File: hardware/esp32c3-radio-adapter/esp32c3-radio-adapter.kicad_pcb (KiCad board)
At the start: 2 copper layers, 27 x 36.5 mm, 7 parts, among them J1 Conn_01x08, J2 Conn_01x08, J3 SX1278_Ra-02

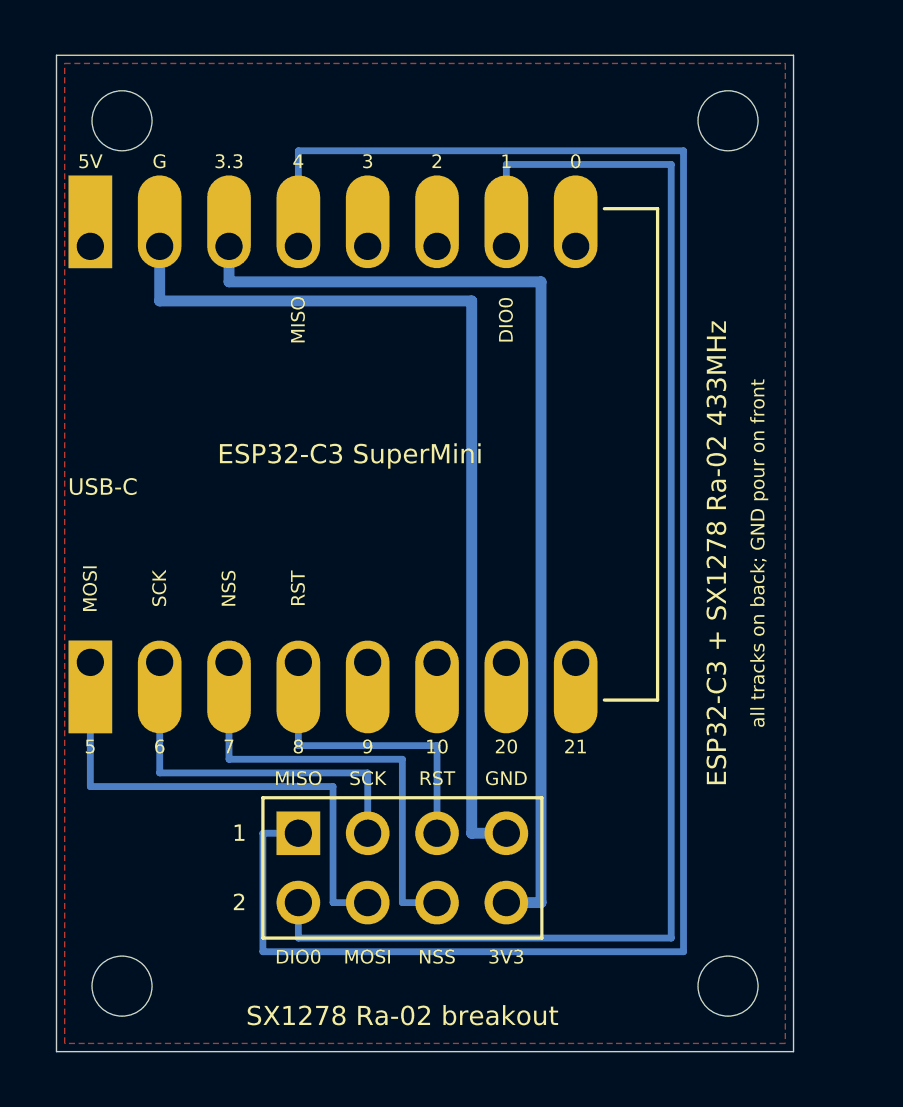
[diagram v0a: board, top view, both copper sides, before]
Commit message: Merge the two socket adapters into esp32c3-radio-adapter; two-sided pin silk on the replicas
* esp32c3-radio-adapter replaces esp32c3-cc1101-adapter and
  esp32c3-ra02-adapter: the E07-M1101D and Ra-02 breakout headers differ
  only at outer column 3 (GDO0 / RST) and inner column 1 (GDO2 / DIO0),
  wired to GPIO10 and GPIO3, so one socket takes either board.  Nets are
  named GDO0_RST, GDO2_DIO0 and CSN_NSS; the silk carries the E07 names
  with the Ra-02 names in parentheses, plus both boards' fab outlines.
* Ra-02 breakout replica: header and module pin numbers on the back silk;
  header pin names beside each column on both sides.
* E07-M1101D replica: pin names beside each column on both sides; the
  markers, box and legend are mirrored onto the back.
* Pinout diagrams combined into docs/images/pinout-radio-boards.svg.
* README, export defaults and generator lists updated.

Co-Authored-By: Claude Fable 5.1 <noreply@anthropic.com>
Claude-Session: https://claude.ai/code/session_01JoGdh4Cg3VtTTDZi4gQuiN
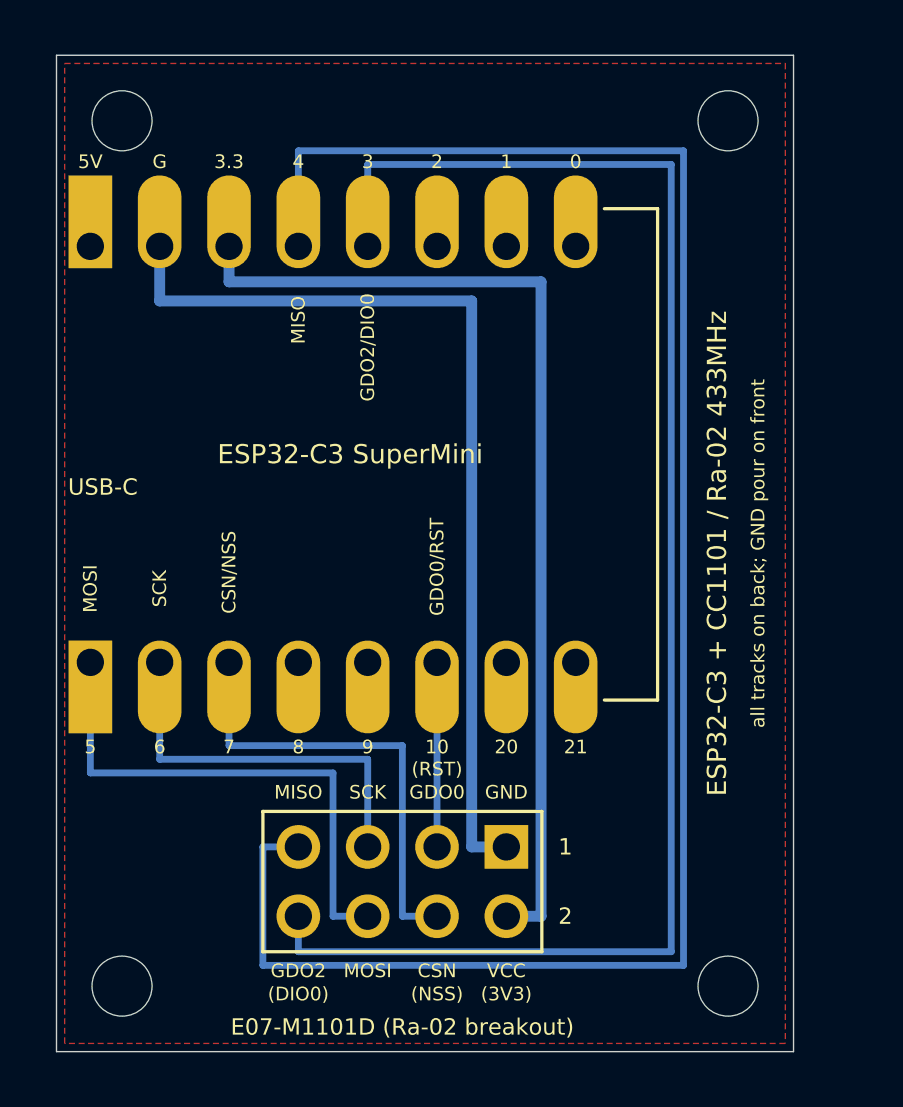
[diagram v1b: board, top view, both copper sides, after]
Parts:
- J3: value SX1278_Ra-02 -> E07-M1101D_or_Ra-02; footprint Adapter:PinSocket_2x04_P2.54mm_Ra02_Breakout -> Adapter:PinSocket_2x04_P2.54mm_E07
- moved J3 7.64 mm to (116.5, 129.0)
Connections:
- J1 pad 3: NSS -> CSN_NSS
- J1 pad 4: RESET -> GPIO8
- J1 pad 6: GPIO10 -> GDO0_RST
- J2 pad 5: GPIO3 -> GDO2_DIO0
- J2 pad 7: DIO0 -> GPIO1
- J3 pad 1: MISO -> GND
- J3 pad 2: DIO0 -> +3V3
- J3 pad 3: SCK -> GDO0_RST
- J3 pad 4: MOSI -> CSN_NSS
- J3 pad 5: RESET -> SCK
- J3 pad 6: NSS -> MOSI
- J3 pad 7: GND -> MISO
- J3 pad 8: +3V3 -> GDO2_DIO0
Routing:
- net GDO2_DIO0: track 0.00 -> 57.9 mm
- net DIO0: track 52.3 -> 0.00 mm
- net CSN_NSS: track 0.00 -> 16.9 mm
- net NSS: track 16.4 -> 0.00 mm
- net RESET: track 11.3 -> 0.00 mm
- net GDO0_RST: track 0.00 -> 6.76 mm
- net SCK: track 13.9 -> 14.4 mm
- net MOSI: track 19.0 -> 19.5 mm
- net MISO: track 68.0 -> 68.5 mm
- net GND: track 34.2 -> 34.7 mm
- net +3V3: track 36.7 -> 37.2 mm
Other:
- board text added: "(3V3)"
- board text added: "(DIO0)"
- board text added: "(NSS)"
- board text added: "(RST)"
- board text added: "CSN"
- board text added: "CSN/NSS"
- board text added: "E07-M1101D (Ra-02 breakout)"
- board text added: "ESP32-C3 + CC1101 / Ra-02 433MHz"
- board text added: "GDO0"
- board text added: "GDO0/RST"
- board text added: "GDO2"
- board text added: "GDO2/DIO0"
- board text added: "VCC"
- board text removed: "3V3"
- board text removed: "DIO0"
- board text removed: "ESP32-C3 + SX1278 Ra-02 433MHz"
- board text removed: "NSS"
- board text removed: "RST"
- board text removed: "SX1278 Ra-02 breakout"

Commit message: Adapters: expansion header for the unused SuperMini pins and a radio-type strap
Pin-header adapter:
* J4, a 1x7 2.54 mm header on the top edge, carries every SuperMini pin the
  radio does not use: 5V, GPIO8, GPIO9, GPIO2, GPIO20, GPIO21, GPIO0.  Its
  pins sit at the gaps between the SuperMini's pins so each net reaches it on
  the front copper without crossing another (power-row nets jog above their
  row, GPIO-row nets rise between the rows and pass between the power-row
  pads).  The radio tracks on the back are unchanged; the GND pour flows
  around the new tracks.
* JP1, a two-pad solder jumper right of the SuperMini, straps GPIO1 (net
  RADIO_ID) to GND: open = CC1101 E07-M1101D, bridged = Ra-02 breakout.

SX1278 module adapter: GPIO1 is tied to 3V3 (silk "ID=3V3"), so the same
pin reads high there.  Firmware samples GPIO1 with the internal pull-down
and then the pull-up to tell the three states apart; GPIO1 is not a boot
strapping pin.

The header is 2.3 mm from the top edge so the MISO lane on the back keeps
its clearance under it.  Both adapters pass ERC and DRC; README and the
manufacturing notes describe the header and the strap.

Co-Authored-By: Claude Fable 5.1 <noreply@anthropic.com>
Claude-Session: https://claude.ai/code/session_01JoGdh4Cg3VtTTDZi4gQuiN
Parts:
- added J4: Expansion, Adapter:PinHeader_1x07_P2.54mm_Vertical, F.Cu at (105.0, 102.3)
- added JP1: RA-02, Adapter:SolderJumper-2_P1.3mm_Open_Pad1.2x1.0mm, F.Cu at (122.9, 110.0)
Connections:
- J2 pad 7: GPIO1 -> RADIO_ID
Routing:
- net GPIO9: track 0.00 -> 21.2 mm
- net GPIO20: track 0.00 -> 21.2 mm
- net GPIO8: track 0.00 -> 21.2 mm
- net GPIO21: track 0.00 -> 21.2 mm
- net RADIO_ID: track 0.00 -> 20.8 mm
- net +5V: track 0.00 -> 8.51 mm
- net GPIO0: track 0.00 -> 5.97 mm
- net GPIO2: track 0.00 -> 5.97 mm
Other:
- board text added: "RA-02 strap"
- board text added: "RADIO_ID"
- board text added: "radio tracks on back; GND pour on front"
- board text added: "radio tracks this side"
- board text removed: "all tracks on back; GND pour on front"
- board text removed: "all tracks this side"

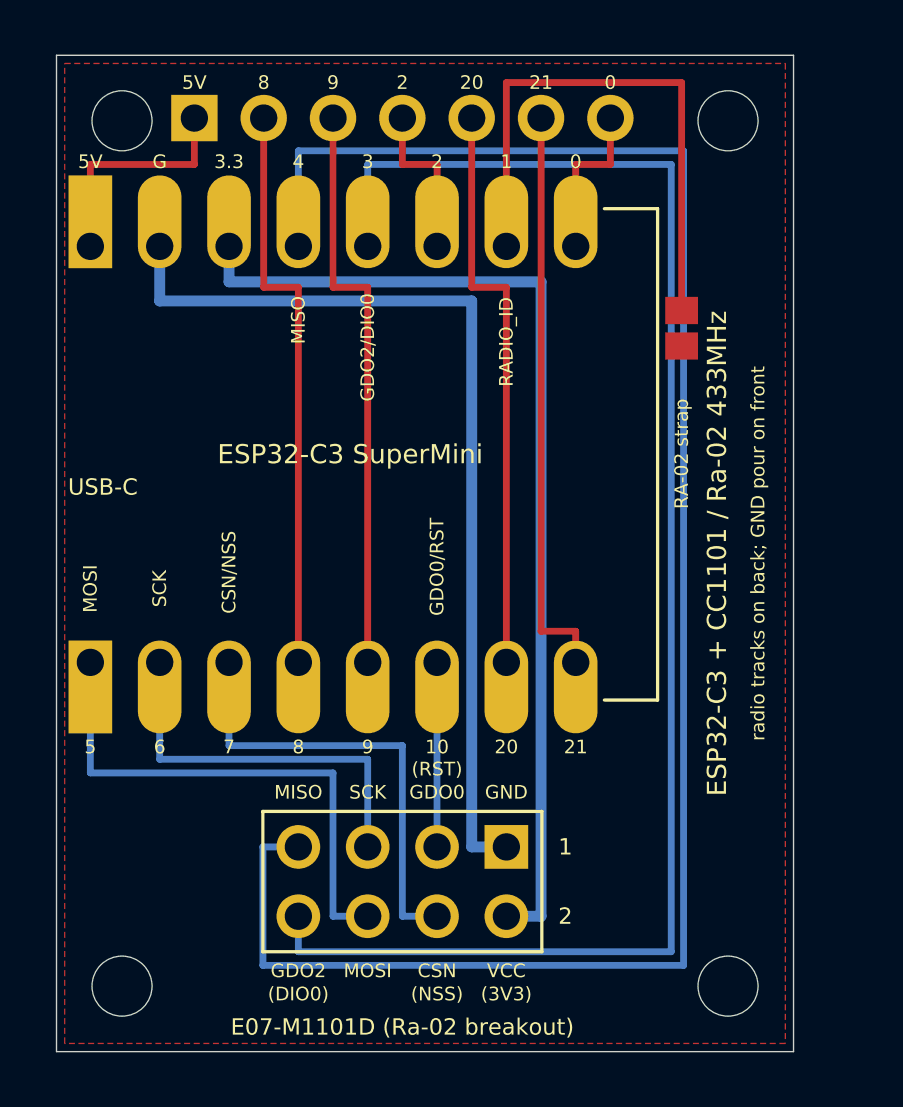
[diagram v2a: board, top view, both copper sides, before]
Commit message: Radio adapter: strap as a jumper header plus 0805 resistor; expansion header centred
* JP1 is now a 1x2 2.54 mm header for an ordinary jumper, with R1 (0805 pads,
  0R) in parallel as the permanent alternative; both take RADIO_ID (GPIO1)
  to GND.  They sit on the front beside the socket, past the SuperMini's
  antenna end so a jumper cap clears it, and right of the MISO/GDO2 descents
  on the back, which widens the board to 29 x 36.5 mm.
* J4 (the unused-pin header) is centred between the top mounting holes, its
  pin order now 5V, 8, 9, 2, 20, 0, 21.  RADIO_ID leaves the power row
  downward through the gap between GPIO-row pins 7 and 8 and runs under
  that row to JP1; GPIO21 goes round the right of the SuperMini to the last
  header pin, so the front routes still do not cross.

Co-Authored-By: Claude Fable 5.1 <noreply@anthropic.com>
Claude-Session: https://claude.ai/code/session_01JoGdh4Cg3VtTTDZi4gQuiN
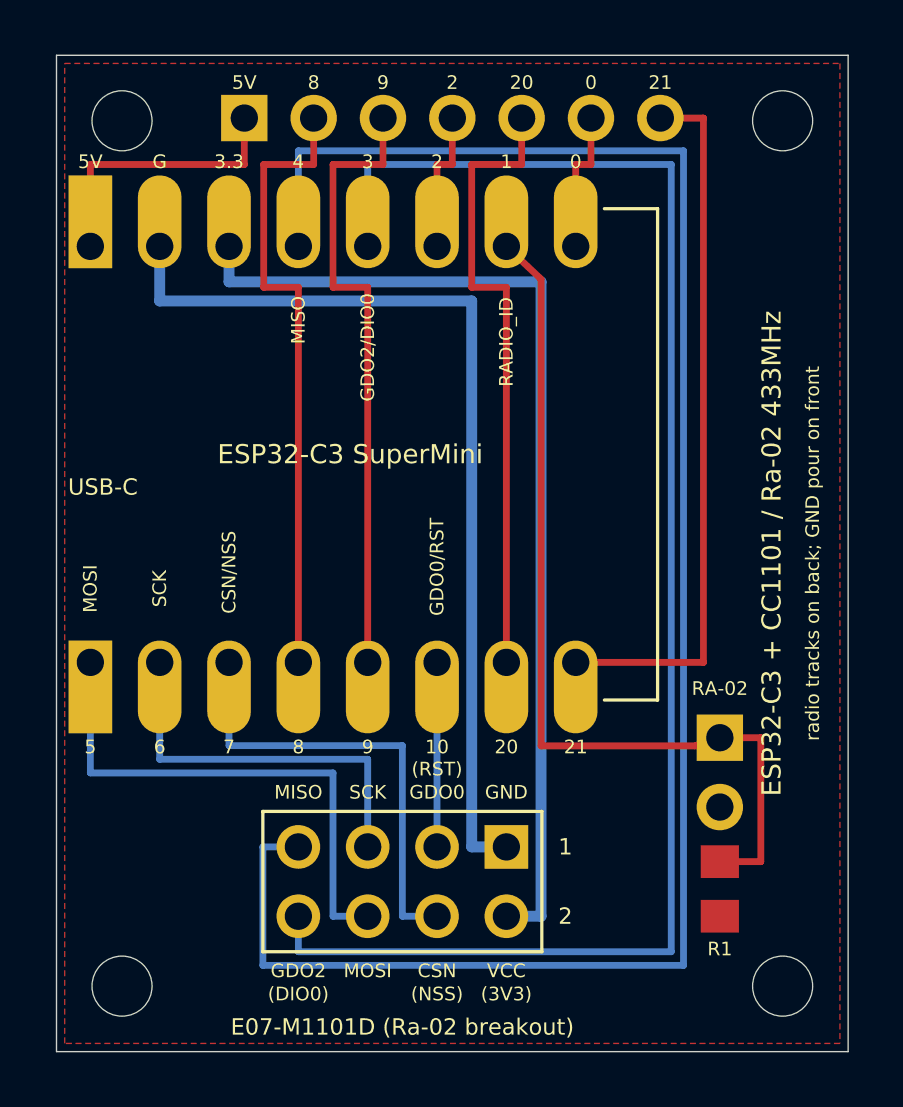
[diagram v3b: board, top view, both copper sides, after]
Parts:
- added R1: 0R, Adapter:R_0805_2012Metric_HandSolder_AlongY, F.Cu at (124.3, 130.5)
- JP1: footprint Adapter:SolderJumper-2_P1.3mm_Open_Pad1.2x1.0mm -> Adapter:PinHeader_1x02_P2.54mm_Vertical_AlongY
- moved JP1 15.1 mm to (124.3, 125.0)
- moved H2 2.00 mm to (126.6, 102.4)
- moved H4 2.00 mm to (126.6, 134.1)
- moved J4 1.83 mm to (106.9, 102.3)
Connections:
- J4 pad 6: GPIO21 -> GPIO0
- J4 pad 7: GPIO0 -> GPIO21
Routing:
- net RADIO_ID: track 20.8 -> 33.0 mm
- net GPIO21: track 21.2 -> 26.2 mm
- net GPIO20: track 21.2 -> 23.0 mm
- net GPIO9: track 21.2 -> 23.0 mm
- net GPIO8: track 21.2 -> 23.0 mm
- net +5V: track 8.51 -> 10.3 mm
- net GPIO0: track 5.97 -> 5.26 mm
- net GPIO2: track 5.97 -> 5.26 mm
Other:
- board size 27 x 36.5 mm -> 29 x 36.5 mm
- board text added: "R1"
- board text added: "RA-02"
- board text removed: "RA-02 strap"

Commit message: Adapters: reassign the GPIOs so the socket adapter routes on one layer
The pin-header (socket) adapter is now entirely on the back copper, the
expansion header and strap included; the front carries only pads and the
GND pour.  New assignment, shared by both adapters:

  MOSI GPIO8, SCK GPIO9, CSN/NSS GPIO0, MISO GPIO7, GDO0/RST(DIO0) GPIO10,
  GDO2/DIO0(DIO1) GPIO6, strap RADIO_ID GPIO5, SX1278 module RESET GPIO4.

GPIO8/9 are boot strapping pins but carry only ESP32 outputs, which float
at boot; the radio's outputs stay on plain GPIOs.  On the socket adapter
the radio signals then all leave the GPIO row, which faces the socket, in
the order its pads want them: GDO0 and SCK drop straight in, MOSI and MISO
via one lane each, GDO2 round the left of the socket into its pad from
below.  CSN/NSS (GPIO0, the last power-row pin) passes under its own pad,
crosses between the rows (now otherwise empty) and drops through a
GPIO-row gap.  GND and 3V3 leave the power row upward, run along the top
edge above the header and down the strip right of the SuperMini into the
socket's right column; GND continues under the socket to the strap.

Expansion header J4 (centred): 3V3, GPIO4, 3, 2, 1, 21, 20 - GPIO4..1 rise
straight up, GPIO21/20 come up the right-hand strip.  5V is dropped: its
pad sits under the top-left hole and cannot be reached on one layer.  The
strap moves to the bottom-left corner (JP1 header, R1 0805 on the back),
fed by GPIO5 dropping straight down and by the under-socket GND lane.

SX1278 module adapter: same map; its GPIO order matches the module's pad
order so the front-copper lanes stay nested; NSS and RESET now come from
the right column on the back copper, 3V3 goes down the right of the
SuperMini, and GPIO5 is tied to 3V3 across the top.

Both adapters pass ERC and DRC; the antenna keepout starts 1.6 mm inboard
of the power row (was 1.3) to give CSN/NSS its lane under the last pad.

Co-Authored-By: Claude Fable 5.1 <noreply@anthropic.com>
Claude-Session: https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
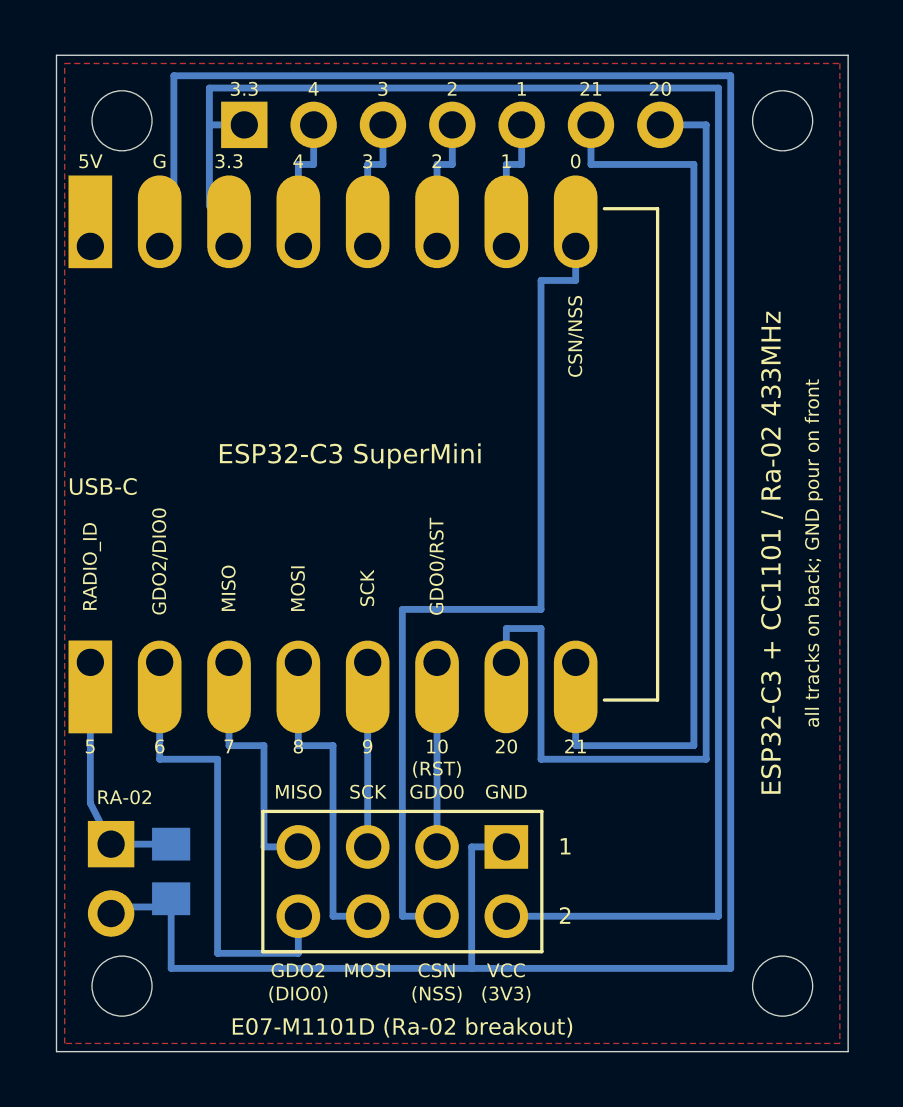
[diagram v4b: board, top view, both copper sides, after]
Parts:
- R1: footprint Adapter:R_0805_2012Metric_HandSolder_AlongY -> Adapter:R_0805_2012Metric_HandSolder_AlongY_Back
- moved JP1 22.6 mm to (102.0, 128.9)
- moved R1 20.1 mm to (104.2, 129.9)
- moved J4 0.25 mm to (106.9, 102.5)
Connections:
- J1 pad 1: MOSI -> RADIO_ID
- J1 pad 2: SCK -> GDO2_DIO0
- J1 pad 3: CSN_NSS -> MISO
- J1 pad 4: GPIO8 -> MOSI
- J1 pad 5: GPIO9 -> SCK
- J2 pad 4: MISO -> GPIO4
- J2 pad 5: GDO2_DIO0 -> GPIO3
- J2 pad 7: RADIO_ID -> GPIO1
- J2 pad 8: GPIO0 -> CSN_NSS
- J4 pad 1: +5V -> +3V3
- J4 pad 2: GPIO8 -> GPIO4
- J4 pad 3: GPIO9 -> GPIO3
- J4 pad 5: GPIO20 -> GPIO1
- J4 pad 6: GPIO0 -> GPIO21
- J4 pad 7: GPIO21 -> GPIO20
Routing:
- net MISO: track 68.5 -> 9.30 mm
- net GND: track 34.7 -> 90.4 mm
- net GDO2_DIO0: track 57.9 -> 17.1 mm
- net +3V3: track 37.2 -> 64.0 mm
- net RADIO_ID: track 33.0 -> 9.04 mm
- net GPIO9: track 23.0 -> 0.00 mm
- net GPIO8: track 23.0 -> 0.00 mm
- net CSN_NSS: track 16.9 -> 32.2 mm
- net GPIO20: track 23.0 -> 38.3 mm
- net +5V: track 10.3 -> 0.00 mm
- net GPIO21: track 26.2 -> 33.9 mm
- net SCK: track 14.4 -> 6.76 mm
- net MOSI: track 19.5 -> 11.8 mm
- net GPIO0: track 5.26 -> 0.00 mm
- net GPIO4: track 0.00 -> 5.01 mm
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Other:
- board text added: "all tracks on back; GND pour on front"
- board text added: "all tracks this side"
- board text removed: "R1"
- board text removed: "radio tracks on back; GND pour on front"
- board text removed: "radio tracks this side"

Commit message: Silk: "3V3" instead of "3.3", and the UART pins named on the spare header
The 3.3 V pin is labelled 3V3 on the SuperMini board and beside the
SuperMini on the adapters, and the expansion header's GPIO21/20 pins read
"21TX" / "20RX".

Co-Authored-By: Claude Fable 5.1 <noreply@anthropic.com>
Claude-Session: https://claude.ai/code/session_01JoGdh4Cg3VtTTDZi4gQuiN
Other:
- board text added: "20RX"
- board text added: "21TX"
- board text added: "3V3"
- board text removed: "3.3"
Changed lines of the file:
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@@
 		)
 	)
-	(gr_text "3.3"
+	(gr_text "3V3"
 		(at 106.32 103.9 0)
 		(layer "F.SilkS")
@@
 		)
 	)
-	(gr_text "3.3"
+	(gr_text "3V3"
 		(at 106.32 103.9 0)
 		(layer "B.SilkS")
@@
 		)
 	)
-	(gr_text "3.3"
+	(gr_text "3V3"
 		(at 106.88 101.25 0)
 		(layer "F.SilkS")
@@
 		)
 	)
-	(gr_text "3.3"
+	(gr_text "3V3"
 		(at 106.88 101.25 0)
 		(layer "B.SilkS")
@@
 		)
 	)
-	(gr_text "21"
+	(gr_text "21TX"
 		(at 119.58 101.25 0)
 		(layer "F.SilkS")
@@
 		)
 	)
-	(gr_text "21"
+	(gr_text "21TX"
 		(at 119.58 101.25 0)
 		(layer "B.SilkS")
@@
 		)
 	)
-	(gr_text "20"
+	(gr_text "20RX"
 		(at 122.12 101.25 0)
 		(layer "F.SilkS")
@@
 		)
 	)
-	(gr_text "20"
+	(gr_text "20RX"
 		(at 122.12 101.25 0)
 		(layer "B.SilkS")
